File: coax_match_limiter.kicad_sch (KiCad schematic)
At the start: 12 parts, among them J3 BNC

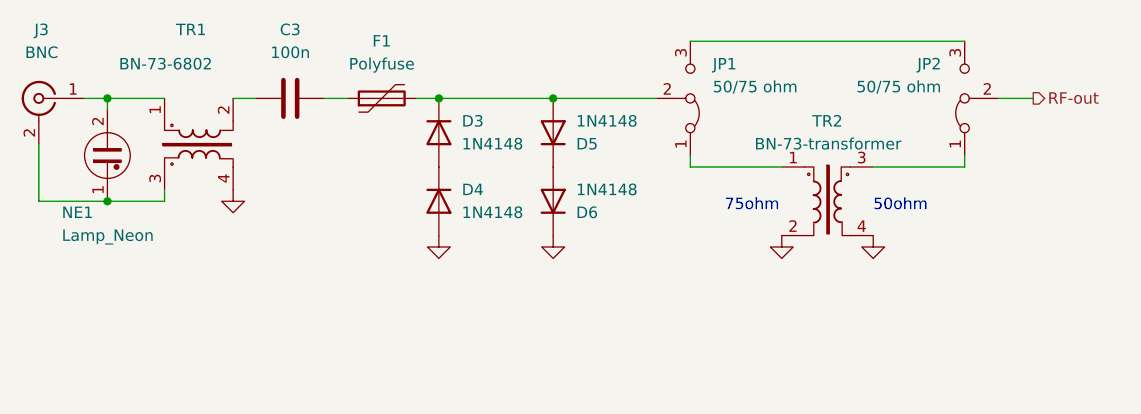
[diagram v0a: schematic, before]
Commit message: changed to 1 to 6
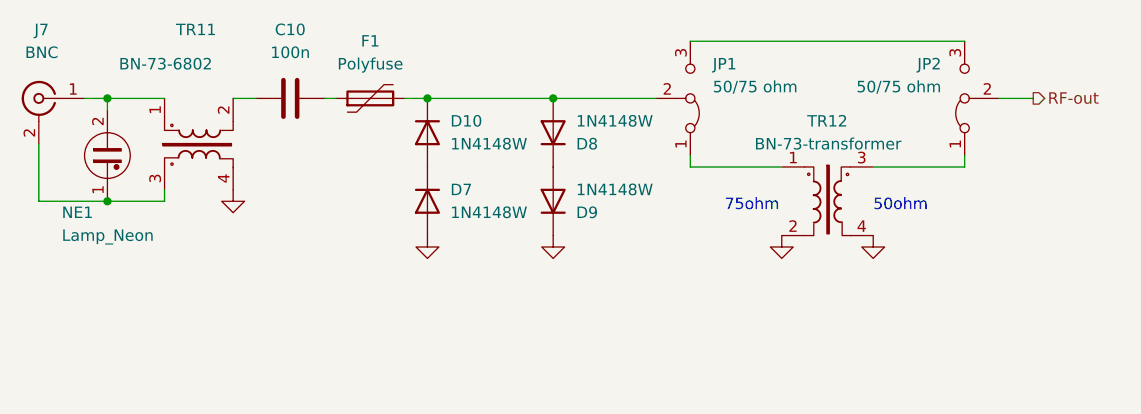
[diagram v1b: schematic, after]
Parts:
- removed D3, D4, D5, D6: 1N4148, Diode_THT:D_DO-35_SOD27_P7.62mm_Horizontal, symbol Diode:1N4148
- added D10, D7, D8, D9: 1N4148W, Diode_SMD:D_SOD-123, symbol Diode:1N4148W
- C10: renamed from C3; footprint Capacitor_THT:C_Disc_D5.1mm_W3.2mm_P5.00mm -> Capacitor_SMD:C_0603_1608Metric_Pad1.08x0.95mm_HandSolder
- renumbered J3 to J7, TR1 to TR11, TR2 to TR12
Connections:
- net GND: now also D7.2 (A), D9.1 (K)
- net at F1.2, JP1.2 (C): now also D10.1 (K), D8.2 (A)
- new net: D8.1 (K), D9.2 (A)
- new net: D10.2 (A), D7.1 (K)
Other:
- moved on the sheet: F1

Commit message: pcb routed and made gerbers
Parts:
- removed JP1, JP2: 50/75 ohm, Connector_PinHeader_2.54mm:PinHeader_1x03_P2.54mm_Vertical, symbol Jumper:Jumper_3_Bridged12
- removed TR12: BN-73-transformer, Components:BN-73-202-1-1, symbol Components:BN-73-transformer
- added J2: limiter, Connector_PinHeader_2.54mm:PinHeader_1x02_P2.54mm_Vertical, symbol Components:Conn_01x02
- J7: footprint Components:BNC_vertical -> Components:BNC_horizontal
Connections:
- net GND: now also TR11.2; no longer TR11.4
- net RF-out: now also F1.2, J2.1 (Pin_1)
- net at J7.1 (In), NE1.2: now also TR11.3; no longer TR11.1
- net at J7.2 (Ext), NE1.1: now also TR11.1; no longer TR11.3
- net at C10.1: now also TR11.4; no longer TR11.2
- net at D10.1 (K), D8.2 (A): now also J2.2 (Pin_2); no longer F1.2
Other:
- note added: "2T"
- note removed: "50ohm"
- note removed: "75ohm"
- moved on the sheet: D10, D7, D8, D9

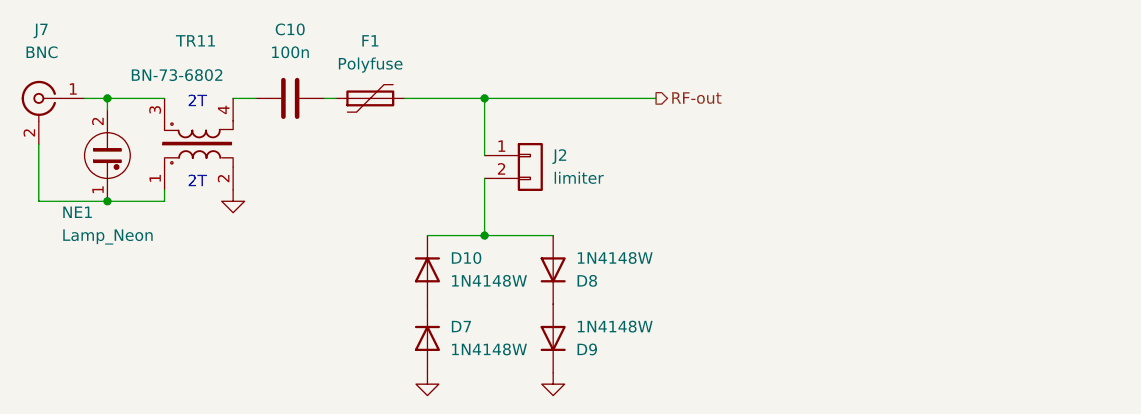
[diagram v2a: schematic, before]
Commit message: changed footprint for 2-way splitter transformer
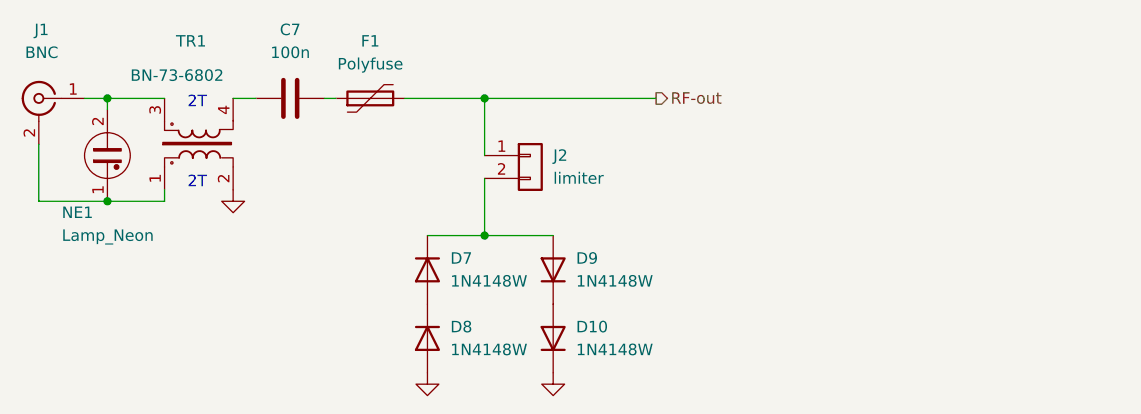
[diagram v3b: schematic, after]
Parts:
- renumbered C10 to C7, D9 to D10, D10 to D7, D7 to D8, D8 to D9, J7 to J1, TR11 to TR1
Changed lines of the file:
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@@
   (symbol (lib_id "Diode:1N4148W") (at 129.54 106.68 90) (unit 1)
     (in_bom yes) (on_board yes) (fields_autoplaced)
-    (property "Reference" "D9" (id 0) (at 132.08 107.9501 90)
+    (property "Reference" "D10" (id 0) (at 132.08 105.4099 90)
       (effects (font (size 1.27 1.27)) (justify right))
     )
-    (property "Value" "1N4148W" (id 1) (at 132.08 105.4101 90)
+    (property "Value" "1N4148W" (id 1) (at 132.08 107.9499 90)
       (effects (font (size 1.27 1.27)) (justify right))
     )
@@
   (symbol (lib_id "power:GND") (at 129.54 110.49 0) (unit 1)
     (in_bom yes) (on_board yes) (fields_autoplaced)
-    (property "Reference" "#PWR015" (id 0) (at 129.54 116.84 0)
+    (property "Reference" "#PWR0137" (id 0) (at 129.54 116.84 0)
       (effects (font (size 1.27 1.27)) hide)
     )
@@
   (symbol (lib_id "Components:BNC") (at 72.39 80.01 0) (mirror y) (unit 1)
     (in_bom yes) (on_board yes) (fields_autoplaced)
-    (property "Reference" "J7" (id 0) (at 72.7074 72.39 0))
+    (property "Reference" "J1" (id 0) (at 72.7074 72.39 0))
     (property "Value" "BNC" (id 1) (at 72.7074 74.93 0))
     (property "Footprint" "Components:BNC_horizontal" (id 2) (at 72.39 80.01 0)
@@
   (symbol (lib_id "Device:C") (at 100.33 80.01 90) (unit 1)
     (in_bom yes) (on_board yes) (fields_autoplaced)
-    (property "Reference" "C10" (id 0) (at 100.33 72.39 90))
+    (property "Reference" "C7" (id 0) (at 100.33 72.39 90))
     (property "Value" "100n" (id 1) (at 100.33 74.93 90))
     (property "Footprint" "Capacitor_SMD:C_0603_1608Metric_Pad1.08x0.95mm_HandSolder" (id 2) (at 104.14 79.0448 0)
@@
   (symbol (lib_id "Diode:1N4148W") (at 115.57 106.68 90) (mirror x) (unit 1)
     (in_bom yes) (on_board yes) (fields_autoplaced)
-    (property "Reference" "D7" (id 0) (at 118.11 105.4099 90)
+    (property "Reference" "D8" (id 0) (at 118.11 105.4099 90)
       (effects (font (size 1.27 1.27)) (justify right))
     )
@@
   (symbol (lib_id "Components:BN-73-transformer") (at 86.36 90.17 90) (unit 1)
     (in_bom yes) (on_board yes)
-    (property "Reference" "TR11" (id 0) (at 87.63 73.66 90)
+    (property "Reference" "TR1" (id 0) (at 87.63 73.66 90)
       (effects (font (size 1.27 1.27)) (justify right))
     )
@@
   (symbol (lib_id "power:GND") (at 115.57 110.49 0) (unit 1)
     (in_bom yes) (on_board yes) (fields_autoplaced)
-    (property "Reference" "#PWR014" (id 0) (at 115.57 116.84 0)
+    (property "Reference" "#PWR0136" (id 0) (at 115.57 116.84 0)
       (effects (font (size 1.27 1.27)) hide)
     )
@@
   (symbol (lib_id "Diode:1N4148W") (at 129.54 99.06 90) (unit 1)
     (in_bom yes) (on_board yes) (fields_autoplaced)
-    (property "Reference" "D8" (id 0) (at 132.08 100.3301 90)
+    (property "Reference" "D9" (id 0) (at 132.08 97.7899 90)
       (effects (font (size 1.27 1.27)) (justify right))
     )
-    (property "Value" "1N4148W" (id 1) (at 132.08 97.7901 90)
+    (property "Value" "1N4148W" (id 1) (at 132.08 100.3299 90)
       (effects (font (size 1.27 1.27)) (justify right))
     )
@@
   (symbol (lib_id "power:GND") (at 93.98 90.17 0) (unit 1)
     (in_bom yes) (on_board yes) (fields_autoplaced)
-    (property "Reference" "#PWR013" (id 0) (at 93.98 96.52 0)
+    (property "Reference" "#PWR0138" (id 0) (at 93.98 96.52 0)
       (effects (font (size 1.27 1.27)) hide)
     )
@@
   (symbol (lib_id "Diode:1N4148W") (at 115.57 99.06 90) (mirror x) (unit 1)
     (in_bom yes) (on_board yes) (fields_autoplaced)
-    (property "Reference" "D10" (id 0) (at 118.11 97.7899 90)
+    (property "Reference" "D7" (id 0) (at 118.11 97.7899 90)
       (effects (font (size 1.27 1.27)) (justify right))
     )
